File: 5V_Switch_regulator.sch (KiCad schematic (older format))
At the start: 13 parts, among them U4 MAX17502F, U9 AP2210N-3.3

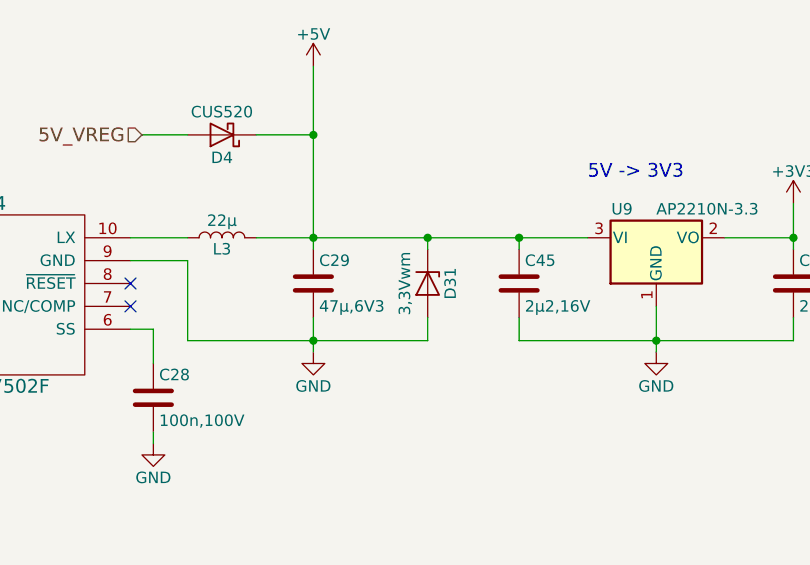
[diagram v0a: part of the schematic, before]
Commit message: 0.2 HW files finalized and repo cleaned up.
-BOM is now up-to-date and available in .csv and .pdf formats
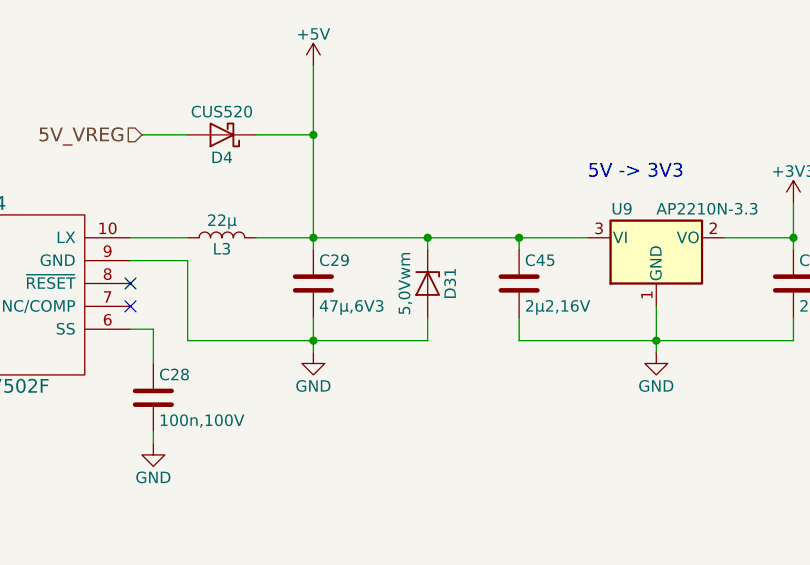
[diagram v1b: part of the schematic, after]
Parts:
- D31: value 3,3Vwm -> 5,0Vwm; MFG SMF3.3 -> SMF5.0
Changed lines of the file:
@@
 P 7550 3600
 F 0 "D31" H 7550 3700 50  0000 C CNN
-F 1 "3,3Vwm" H 7550 3500 50  0000 C CNN
+F 1 "5,0Vwm" H 7550 3500 50  0000 C CNN
 F 2 "Diodes_SMD:D_SOD-123F" H 7550 3600 50  0001 C CNN
 F 3 "" H 7550 3600 50  0001 C CNN
-F 4 "SMF3.3" H 7550 3600 60  0001 C CNN "MFG"
+F 4 "SMF5.0" H 7550 3600 60  0001 C CNN "MFG"
 	1    7550 3600
 	0    1    1    0
